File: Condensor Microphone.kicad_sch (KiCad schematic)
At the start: 12 parts, among them U3 MAX9814

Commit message: getting closer
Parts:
- removed C17: 10U, Capacitor_SMD:C_0805_2012Metric, symbol Device:C
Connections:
- net at U3.6 (MICOUT): now also R23.2
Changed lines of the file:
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@@
   (junction (at 92.075 95.25) (diameter 0) (color 0 0 0 0)
   )
-  (wire (pts (xy 179.07 95.25) (xy 182.88 95.25))
-    (stroke (width 0) (type default))
-  )
   (wire (pts (xy 120.015 117.475) (xy 120.015 116.205))
     (stroke (width 0) (type default))
@@
     (stroke (width 0) (type default))
   )
-  (wire (pts (xy 167.64 95.25) (xy 171.45 95.25))
+  (wire (pts (xy 167.64 95.25) (xy 182.88 95.25))
     (stroke (width 0) (type default))
   )
@@
         )
       )
-    )
-  )
-  (symbol (lib_id "Device:C") (at 175.26 95.25 270) (unit 1)
-    (in_bom yes) (on_board yes) (dnp no)
-    (property "Reference" "C17" (at 175.26 101.6 90)
-      (effects (font (size 1.27 1.27)))
-    )
-    (property "Value" "10U" (at 173.355 99.06 90)
-      (effects (font (size 1.27 1.27)))
-    )
-    (property "Footprint" "Capacitor_SMD:C_0805_2012Metric" (at 171.45 96.2152 0)
-      (effects (font (size 1.27 1.27)) hide)
-    )
-    (property "Datasheet" "~" (at 175.26 95.25 0)
-      (effects (font (size 1.27 1.27)) hide)
-    )
-    (property "Specs" "0805" (at 179.07 99.06 90)
-      (effects (font (size 1.27 1.27)))
-    )
-    (pin "1")
-    (pin "2")
-    (instances
-      (project "DaisySeedBreakout"
-        (path "/a83c9f4b-f61b-47d4-b39d-4636bff6eb0e"
-          (reference "C17") (unit 1)
-        )
-        (path "/a83c9f4b-f61b-47d4-b39d-4636bff6eb0e/33b46824-2cf1-41f4-ab61-a56b9cf41949"
-          (reference "C23") (unit 1)
-        )
-      )

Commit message: partially routed
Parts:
- removed C12: 0.1uF, Capacitor_SMD:C_0402_1005Metric, symbol Device:C
- removed C13: 0.47uF, Capacitor_SMD:C_0402_1005Metric, symbol Device:C
- removed C14: 2.2uF, Capacitor_SMD:C_0603_1608Metric, symbol Device:C
- removed C15: 470nF, Capacitor_SMD:C_0402_1005Metric, symbol Device:C
- removed C16: 1uF, Capacitor_SMD:C_0402_1005Metric, symbol Device:C
- removed MK1: Microphone_Condenser, microphone:MIC_AOM-6545_PUI, symbol Device:Microphone_Condenser
- removed R21, R22: 150k, Resistor_SMD:R_0402_1005Metric, symbol Device:R_US
- removed R5: 2.21k, Resistor_SMD:R_0402_1005Metric, symbol Device:R_US
- removed U3: MAX9814, Package_DFN_QFN:DFN-14-1EP_3x3mm_P0.4mm_EP1.78x2.35mm, symbol Amplifier_Audio:MAX9814
- added C16: 1uF, Capacitor_SMD:C_0603_1608Metric, symbol Device:C
- added C16 (x2): 0.1uF, Capacitor_SMD:C_0402_1005Metric, symbol Device:C
- added C16: 0.01uF, Capacitor_SMD:C_0402_1005Metric, symbol Device:C
- added C16: 100pF, Capacitor_SMD:C_0402_1005Metric, symbol Device:C
- added J16: Conn_01x02, 1x2FemaleVertical:PinHeader_1x02_P2.54mm_VerticalFemale, symbol 4ms_Connector:Conn_01x02
- added R5 (x2): 1M, Resistor_SMD:R_0402_1005Metric, symbol Device:R_US
- added R5: 10k, Resistor_SMD:R_0402_1005Metric, symbol Device:R_US
- added R5: 100k, Resistor_SMD:R_0402_1005Metric, symbol Device:R_US
- added R5 (x2): 2k, Resistor_SMD:R_0402_1005Metric, symbol Device:R_US
- added U2: MAX4466EXK_T, digikey-footprints:SOT-353, symbol dk_Linear-Amplifiers-Audio:MAX4466EXK_T
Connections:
- net GND: now also C16.1, C16.2, C16.2, J16.2 (Pin_2), R5.1, U2.2 (GND)
- net VCC_2V7_to_5V5: now also C16.1, R5.2, R5.2, U2.5 (VCC)
- net at R23.2: now also C16.2, R5.1, U2.4
- new net: C16.2, R5.1
- new net: C16.1, J16.1 (Pin_1), R5.1
- new net: C16.2, R5.1, R5.2, U2.1
- new net: C16.1, R5.2, R5.2, U2.3
- new net: C16.1, R5.1, R5.2
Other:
- note added: "Electret Microphone Plugs in here."

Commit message: periodic update
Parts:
- removed R23: 4.7k, Resistor_SMD:R_0402_1005Metric, symbol Device:R_US
- J16: footprint 1x2FemaleVertical:PinHeader_1x02_P2.54mm_VerticalFemale -> HeadersWithSolderHoles:PinHeader_1x02_P2.54mm_VerticalFemale_WithSolderHoles
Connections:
- net AUDIO_OUT: now also C16.2, R5.1, U2.4
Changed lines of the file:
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@@
   (junction (at 100.584 85.852) (diameter 0) (color 0 0 0 0)
-  )
-  (junction (at 165.862 100.838) (diameter 0) (color 0 0 0 0)
   )
   (junction (at 121.92 103.378) (diameter 0) (color 0 0 0 0)
@@
   )
   (junction (at 100.584 103.378) (diameter 0) (color 0 0 0 0)
+  )
+  (junction (at 165.862 100.838) (diameter 0) (color 0 0 0 0)
   )
   (wire (pts (xy 152.146 80.01) (xy 152.146 84.074))
@@
     (stroke (width 0) (type default))
   )
-  (wire (pts (xy 173.482 100.838) (xy 177.292 100.838))
+  (wire (pts (xy 165.862 100.838) (xy 177.292 100.838))
     (stroke (width 0) (type default))
   )
@@
     (effects (font (size 1.27 1.27)) (justify left))
   )
-  (symbol (lib_id "Device:R_US") (at 169.672 100.838 270) (unit 1)
-    (in_bom yes) (on_board yes) (dnp no)
-    (property "Reference" "R23" (at 170.307 104.648 90)
-      (effects (font (size 1.27 1.27)))
-    )
-    (property "Value" "4.7k" (at 170.307 102.743 90)
-      (effects (font (size 1.27 1.27)))
-    )
-    (property "Footprint" "Resistor_SMD:R_0402_1005Metric" (at 169.418 101.854 90)
-      (effects (font (size 1.27 1.27)) hide)
-    )
-    (property "Datasheet" "~" (at 169.672 100.838 0)
-      (effects (font (size 1.27 1.27)) hide)
-    )
-    (property "Specks" "0402" (at 173.482 102.743 90)
-      (effects (font (size 1.27 1.27)) hide)
-    )
-    (pin "1")
-    (pin "2")
-    (instances
-      (project "DaisySeedBreakout"
-        (path "/a83c9f4b-f61b-47d4-b39d-4636bff6eb0e"
-          (reference "R23") (unit 1)
-        )
-        (path "/a83c9f4b-f61b-47d4-b39d-4636bff6eb0e/33b46824-2cf1-41f4-ab61-a56b9cf41949"
-          (reference "R29") (unit 1)
-        )
-      )
-    )
-  )
   (symbol (lib_id "Device:C") (at 135.128 94.488 180) (unit 1)
     (in_bom yes) (on_board yes) (dnp no)
@@
       (effects (font (size 1.27 1.27)) hide)
     )
-    (property "Footprint" "1x2FemaleVertical:PinHeader_1x02_P2.54mm_VerticalFemale" (at 95.885 104.521 0)
+    (property "Footprint" "HeadersWithSolderHoles:PinHeader_1x02_P2.54mm_VerticalFemale_WithSolderHoles" (at 95.885 104.521 0)
       (effects (font (size 1.27 1.27)) hide)
     )

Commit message: Layout routed, no DRC yet
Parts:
- J16: footprint HeadersWithSolderHoles:PinHeader_1x02_P2.54mm_VerticalFemale_WithSolderHoles -> 1x2FemaleVertical:PinHeader_1x02_P2.54mm_VerticalFemale
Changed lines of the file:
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@@
       (effects (font (size 1.27 1.27)) hide)
     )
-    (property "Footprint" "HeadersWithSolderHoles:PinHeader_1x02_P2.54mm_VerticalFemale_WithSolderHoles" (at 95.885 104.521 0)
+    (property "Footprint" "1x2FemaleVertical:PinHeader_1x02_P2.54mm_VerticalFemale" (at 95.885 104.521 0)
       (effects (font (size 1.27 1.27)) hide)
     )

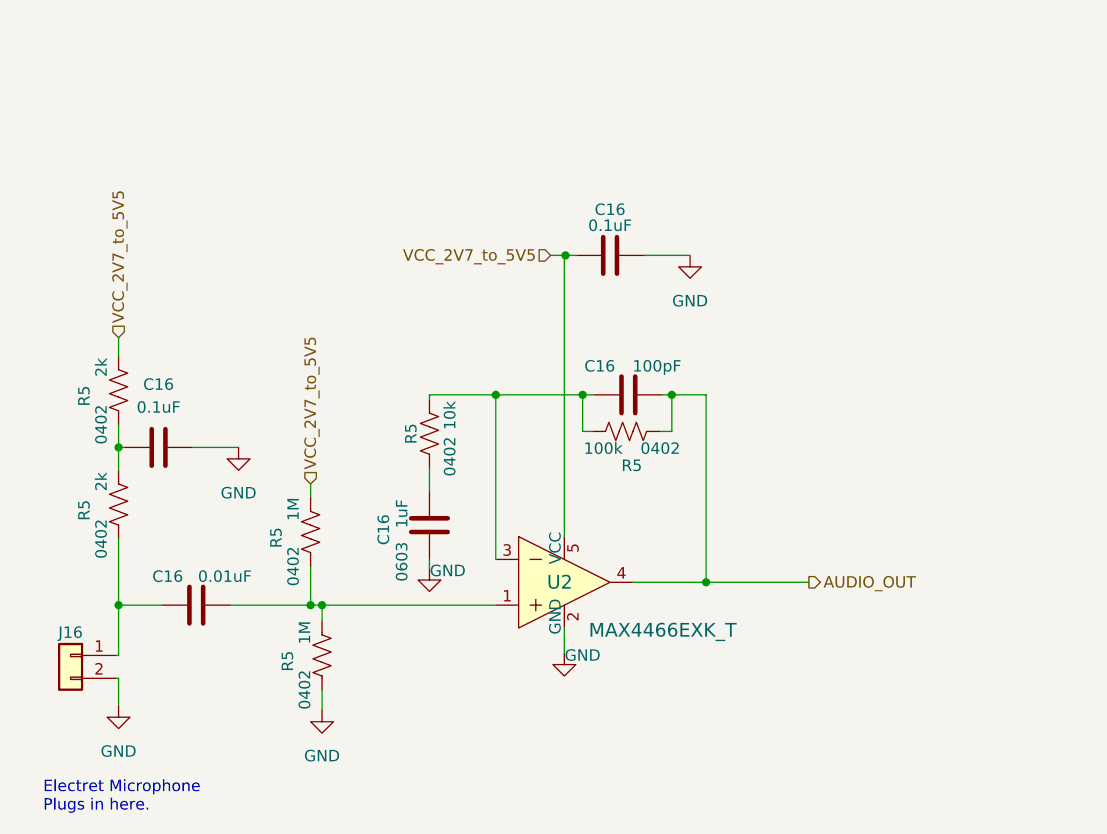
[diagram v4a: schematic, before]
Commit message: PCB cleanup, added accelerometer as easy sensor to begin with
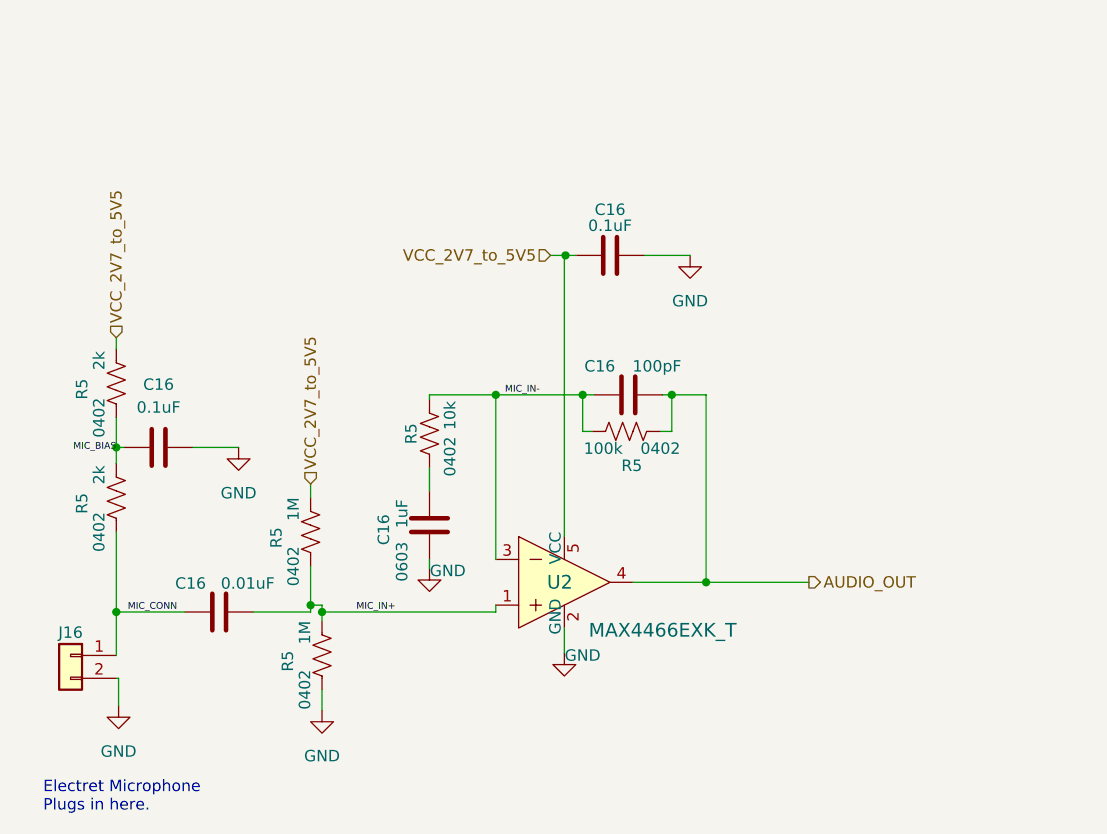
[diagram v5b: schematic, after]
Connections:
- net MIC_CONN: now reaches C16.1, J16.1 (Pin_1), R5.1
- net MIC_IN+: now reaches C16.2, R5.1, R5.2, U2.1
- net MIC_IN-: now reaches C16.1, R5.2, R5.2, U2.3
- net MIC_BIAS: now reaches C16.1, R5.1, R5.2
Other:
- moved on the sheet: C16, R5
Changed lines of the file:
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@@
 (kicad_sch (version 20230121) (generator eeschema)
   (paper "A4")
+  (junction (at 123.19 104.14) (diameter 0) (color 0 0 0 0)
+  )
   (junction (at 150.241 64.516) (diameter 0) (color 0 0 0 0)
   )
   (junction (at 142.494 80.01) (diameter 0) (color 0 0 0 0)
   )
-  (junction (at 100.584 85.852) (diameter 0) (color 0 0 0 0)
+  (junction (at 100.33 85.852) (diameter 0) (color 0 0 0 0)
   )
   (junction (at 121.92 103.378) (diameter 0) (color 0 0 0 0)
   )
+  (junction (at 100.33 104.14) (diameter 0) (color 0 0 0 0)
+  )
   (junction (at 152.146 80.01) (diameter 0) (color 0 0 0 0)
   )
-  (junction (at 123.19 103.378) (diameter 0) (color 0 0 0 0)
-  )
   (junction (at 162.052 80.01) (diameter 0) (color 0 0 0 0)
   )
-  (junction (at 100.584 103.378) (diameter 0) (color 0 0 0 0)
-  )
   (junction (at 165.862 100.838) (diameter 0) (color 0 0 0 0)
   )
@@
     (stroke (width 0) (type default))
   )
+  (wire (pts (xy 123.19 104.14) (xy 123.19 103.378))
+    (stroke (width 0) (type default))
+  )
   (wire (pts (xy 165.862 100.838) (xy 157.734 100.838))
     (stroke (width 0) (type default))
@@
     (stroke (width 0) (type default))
   )
-  (wire (pts (xy 100.584 85.852) (xy 101.219 85.852))
+  (wire (pts (xy 121.92 104.14) (xy 121.92 103.378))
     (stroke (width 0) (type default))
   )
@@
     (stroke (width 0) (type default))
   )
-  (wire (pts (xy 100.584 103.378) (xy 100.584 108.966))
-    (stroke (width 0) (type default))
-  )
-  (wire (pts (xy 100.584 96.012) (xy 100.584 103.378))
-    (stroke (width 0) (type default))
-  )
-  (wire (pts (xy 123.19 103.378) (xy 123.19 105.156))
+  (wire (pts (xy 100.33 104.14) (xy 100.33 108.966))
     (stroke (width 0) (type default))
   )
@@
     (stroke (width 0) (type default))
   )
-  (wire (pts (xy 113.03 103.378) (xy 121.92 103.378))
-    (stroke (width 0) (type default))
-  )
-  (wire (pts (xy 100.584 103.378) (xy 105.41 103.378))
-    (stroke (width 0) (type default))
-  )
-  (wire (pts (xy 100.584 83.312) (xy 100.584 85.852))
+  (wire (pts (xy 115.57 104.14) (xy 121.92 104.14))
+    (stroke (width 0) (type default))
+  )
+  (wire (pts (xy 100.33 104.14) (xy 107.95 104.14))
+    (stroke (width 0) (type default))
+  )
+  (wire (pts (xy 100.33 82.55) (xy 100.33 85.852))
     (stroke (width 0) (type default))
   )
@@
     (stroke (width 0) (type default))
   )
-  (wire (pts (xy 100.584 108.966) (xy 100.33 108.966))
-    (stroke (width 0) (type default))
-  )
   (wire (pts (xy 161.036 80.01) (xy 162.052 80.01))
     (stroke (width 0) (type default))
   )
+  (wire (pts (xy 100.33 95.25) (xy 100.33 104.14))
+    (stroke (width 0) (type default))
+  )
+  (wire (pts (xy 100.33 85.852) (xy 101.219 85.852))
+    (stroke (width 0) (type default))
+  )
   (wire (pts (xy 121.92 89.916) (xy 121.92 91.44))
     (stroke (width 0) (type default))
@@
     (stroke (width 0) (type default))
   )
-  (wire (pts (xy 100.584 73.66) (xy 100.584 75.692))
+  (wire (pts (xy 100.33 73.66) (xy 100.33 74.93))
     (stroke (width 0) (type default))
   )
@@
     (stroke (width 0) (type default))
   )
+  (wire (pts (xy 142.494 104.14) (xy 142.494 103.378))
+    (stroke (width 0) (type default))
+  )
+  (wire (pts (xy 123.19 104.14) (xy 123.19 105.156))
+    (stroke (width 0) (type default))
+  )
   (wire (pts (xy 162.052 80.01) (xy 165.862 80.01))
     (stroke (width 0) (type default))
@@
     (stroke (width 0) (type default))
   )
-  (wire (pts (xy 100.584 85.852) (xy 100.584 88.392))
+  (wire (pts (xy 100.33 85.852) (xy 100.33 87.63))
     (stroke (width 0) (type default))
   )
@@
     (stroke (width 0) (type default))
   )
-  (wire (pts (xy 123.19 103.378) (xy 142.494 103.378))
+  (wire (pts (xy 123.19 104.14) (xy 142.494 104.14))
     (stroke (width 0) (type default))
   )
@@
     (effects (font (size 1.27 1.27)) (justify left bottom))
   )
+  (label "MIC_IN-" (at 143.51 80.01 0) (fields_autoplaced)
+    (effects (font (size 0.75 0.75)) (justify left bottom))
+  )
+  (label "MIC_IN+" (at 127 104.14 0) (fields_autoplaced)
+    (effects (font (size 0.75 0.75)) (justify left bottom))
+  )
+  (label "MIC_CONN" (at 101.6 104.14 0) (fields_autoplaced)
+    (effects (font (size 0.75 0.75)) (justify left bottom))
+  )
+  (label "MIC_BIAS" (at 100.33 86.36 180) (fields_autoplaced)
+    (effects (font (size 0.75 0.75)) (justify right bottom))
+  )
   (hierarchical_label "VCC_2V7_to_5V5" (shape input) (at 148.59 64.516 180) (fields_autoplaced)
     (effects (font (size 1.27 1.27)) (justify right))
   )
-  (hierarchical_label "VCC_2V7_to_5V5" (shape input) (at 100.584 73.66 90) (fields_autoplaced)
+  (hierarchical_label "VCC_2V7_to_5V5" (shape input) (at 100.33 73.66 90) (fields_autoplaced)
     (effects (font (size 1.27 1.27)) (justify left))
   )
@@
     )
   )
-  (symbol (lib_id "Device:C") (at 109.22 103.378 90) (unit 1)
-    (in_bom yes) (on_board yes) (dnp no)
-    (property "Reference" "C16" (at 106.045 100.203 90)
-      (effects (font (size 1.27 1.27)))
-    )
-    (property "Value" "0.01uF" (at 112.395 100.203 90)
-      (effects (font (size 1.27 1.27)))
-    )
-    (property "Footprint" "Capacitor_SMD:C_0402_1005Metric" (at 113.03 102.4128 0)
-      (effects (font (size 1.27 1.27)) hide)
-    )
-    (property "Datasheet" "~" (at 109.22 103.378 0)
+  (symbol (lib_id "Device:C") (at 111.76 104.14 90) (unit 1)
+    (in_bom yes) (on_board yes) (dnp no)
+    (property "Reference" "C16" (at 108.585 100.965 90)
+      (effects (font (size 1.27 1.27)))
+    )
+    (property "Value" "0.01uF" (at 114.935 100.965 90)
+      (effects (font (size 1.27 1.27)))
+    )
+    (property "Footprint" "Capacitor_SMD:C_0402_1005Metric" (at 115.57 103.1748 0)
+      (effects (font (size 1.27 1.27)) hide)
+    )
+    (property "Datasheet" "~" (at 111.76 104.14 0)
       (effects (font (size 1.27 1.27)) hide)
     )
@@
     )
   )
-  (symbol (lib_id "Device:R_US") (at 100.584 92.202 180) (unit 1)
-    (in_bom yes) (on_board yes) (dnp no)
-    (property "Reference" "R5" (at 96.774 92.837 90)
-      (effects (font (size 1.27 1.27)))
-    )
-    (property "Value" "2k" (at 98.679 89.662 90)
-      (effects (font (size 1.27 1.27)))
-    )
-    (property "Footprint" "Resistor_SMD:R_0402_1005Metric" (at 99.568 91.948 90)
-      (effects (font (size 1.27 1.27)) hide)
-    )
-    (property "Datasheet" "~" (at 100.584 92.202 0)
-      (effects (font (size 1.27 1.27)) hide)
-    )
-    (property "Specks" "0402" (at 98.679 96.012 90)
+  (symbol (lib_id "Device:R_US") (at 100.33 91.44 180) (unit 1)
+    (in_bom yes) (on_board yes) (dnp no)
+    (property "Reference" "R5" (at 96.52 92.075 90)
+      (effects (font (size 1.27 1.27)))
+    )
+    (property "Value" "2k" (at 98.425 88.9 90)
+      (effects (font (size 1.27 1.27)))
+    )
+    (property "Footprint" "Resistor_SMD:R_0402_1005Metric" (at 99.314 91.186 90)
+      (effects (font (size 1.27 1.27)) hide)
+    )
+    (property "Datasheet" "~" (at 100.33 91.44 0)
+      (effects (font (size 1.27 1.27)) hide)
+    )
+    (property "Specks" "0402" (at 98.425 95.25 90)
       (effects (font (size 1.27 1.27)))
     )
@@
     )
   )
-  (symbol (lib_id "Device:R_US") (at 100.584 79.502 180) (unit 1)
-    (in_bom yes) (on_board yes) (dnp no)
-    (property "Reference" "R5" (at 96.774 80.137 90)
-      (effects (font (size 1.27 1.27)))
-    )
-    (property "Value" "2k" (at 98.679 76.962 90)
-      (effects (font (size 1.27 1.27)))
-    )
-    (property "Footprint" "Resistor_SMD:R_0402_1005Metric" (at 99.568 79.248 90)
-      (effects (font (size 1.27 1.27)) hide)
-    )
-    (property "Datasheet" "~" (at 100.584 79.502 0)
-      (effects (font (size 1.27 1.27)) hide)
-    )
-    (property "Specks" "0402" (at 98.679 83.312 90)
-      (effects (font (size 1.27 1.27)))
-    )
+  (symbol (lib_id "Device:R_US") (at 100.33 78.74 180) (unit 1)
+    (in_bom yes) (on_board yes) (dnp no)
+    (property "Reference" "R5" (at 96.52 79.375 90)
+      (effects (font (size 1.27 1.27)))
+    )
+    (property "Value" "2k" (at 98.425 76.2 90)
+      (effects (font (size 1.27 1.27)))
+    )
+    (property "Footprint" "Resistor_SMD:R_0402_1005Metric" (at 99.314 78.486 90)
+      (effects (font (size 1.27 1.27)) hide)
+    )
+    (property "Datasheet" "~" (at 100.33 78.74 0)
+      (effects (font (size 1.27 1.27)) hide)
+    )
+    (property "Specks" "0402" (at 98.425 82.55 90)
+      (effects (font (size 1.27 1.27)))
+    )

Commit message: some cleanup
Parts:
- C16: MnfNumber (none) -> FCC0603B105K250CT
- C16: value 0.01uF -> 0.1uF
- C16: value 100pF -> 100pF COG; MnfNumber (none) -> HGC0402G0101J500NTEJ
- U2: MnfNumber (none) -> MAX4466EXK+T
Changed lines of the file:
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@@
       (effects (font (size 1.27 1.27)))
+    )
+    (property "MnfNumber" "FCC0603B105K250CT" (at 135.128 94.488 90)
+      (effects (font (size 1.27 1.27)) hide)
     )
     (pin "1")
@@
       (effects (font (size 1.27 1.27)))
     )
-    (property "Value" "0.01uF" (at 114.935 100.965 90)
+    (property "Value" "0.1uF" (at 114.935 100.965 90)
       (effects (font (size 1.27 1.27)))
     )
@@
     (property "Status" "Active" (at 155.194 70.358 0)
       (effects (font (size 1.524 1.524)) (justify left) hide)
+    )
+    (property "MnfNumber" "MAX4466EXK+T" (at 150.114 100.838 0)
+      (effects (font (size 1.27 1.27)) hide)
     )
     (pin "1")
@@
       (effects (font (size 1.27 1.27)))
     )
-    (property "Value" "100pF" (at 160.401 76.835 90)
+    (property "Value" "100pF COG" (at 162.4686 76.7182 90)
       (effects (font (size 1.27 1.27)))
     )
@@
       (effects (font (size 1.27 1.27)) hide)
     )
+    (property "MnfNumber" "HGC0402G0101J500NTEJ" (at 157.226 80.01 90)
+      (effects (font (size 1.27 1.27)) hide)
+    )
